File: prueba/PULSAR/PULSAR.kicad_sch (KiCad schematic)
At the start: 9 parts, among them J1 Conn_01x20, J2 Conn_01x04, J3 USB_C_Receptacle, U1 AP2112K-3.3, U2 SS49E, U3 CD74HC4067M, U4 ADS8688

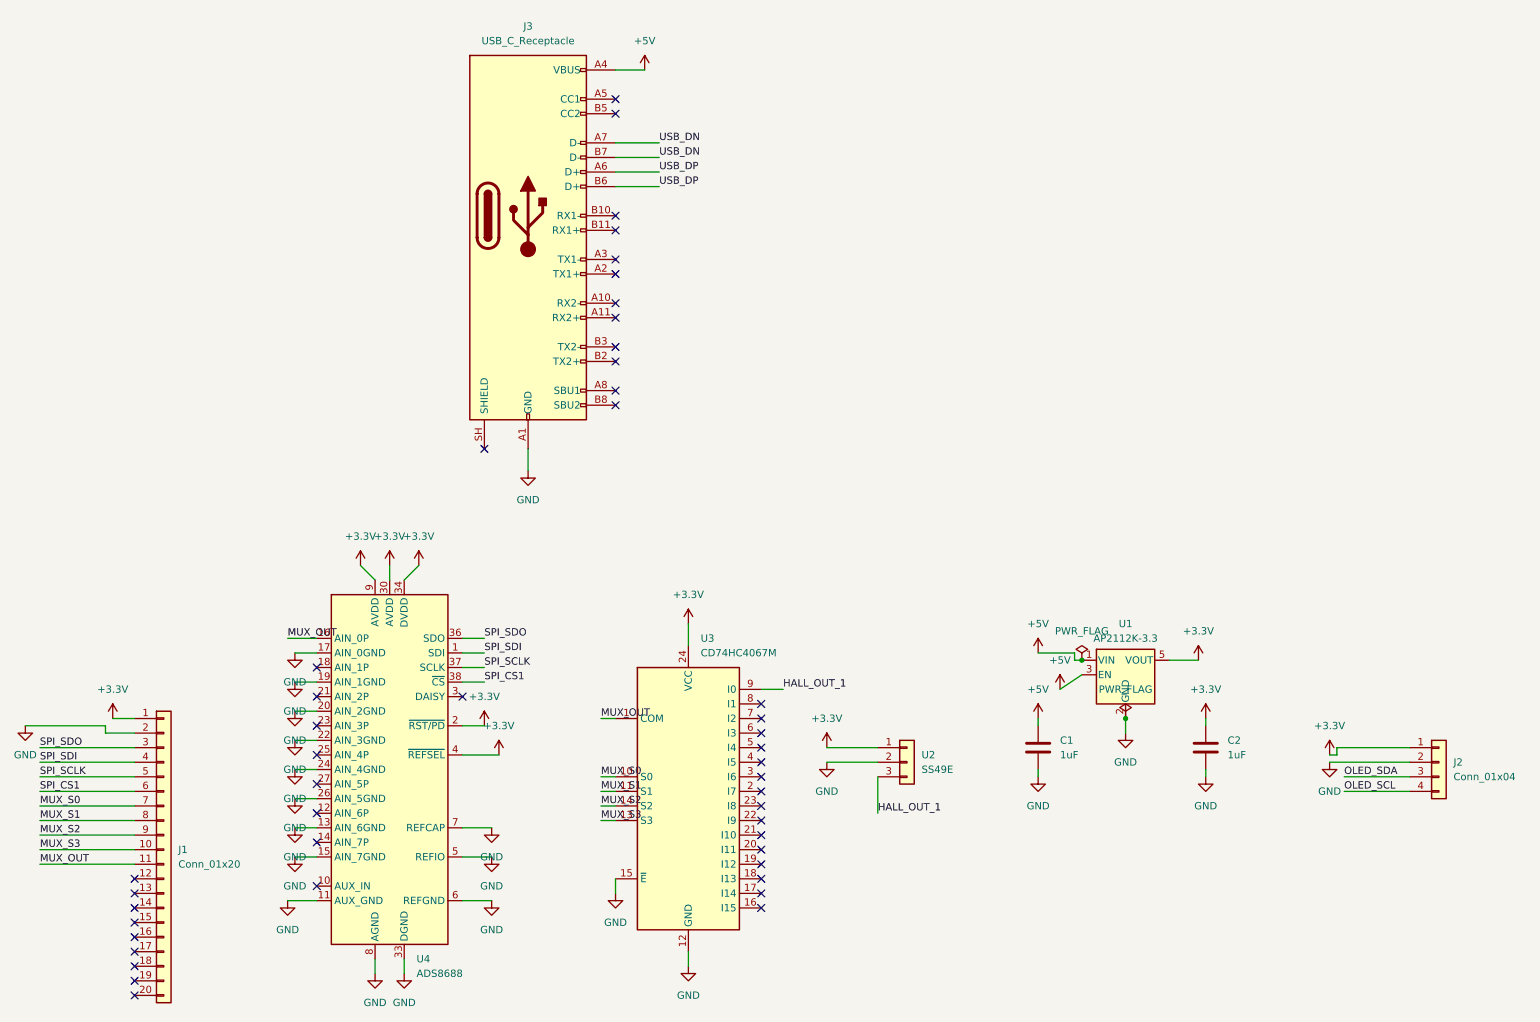
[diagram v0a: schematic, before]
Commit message: Kicad (#11)
* feat: esquemático base completo - USB-C, OLED SPI, OrangeCrab, ADS8688

* feat: complete BOM with verified LCSC part numbers

* feat: PCB routing in progress - power and SPI connections

---------

Co-authored-by: Axel Ibarrondo <135344010+Axel84727@users.noreply.github.com>
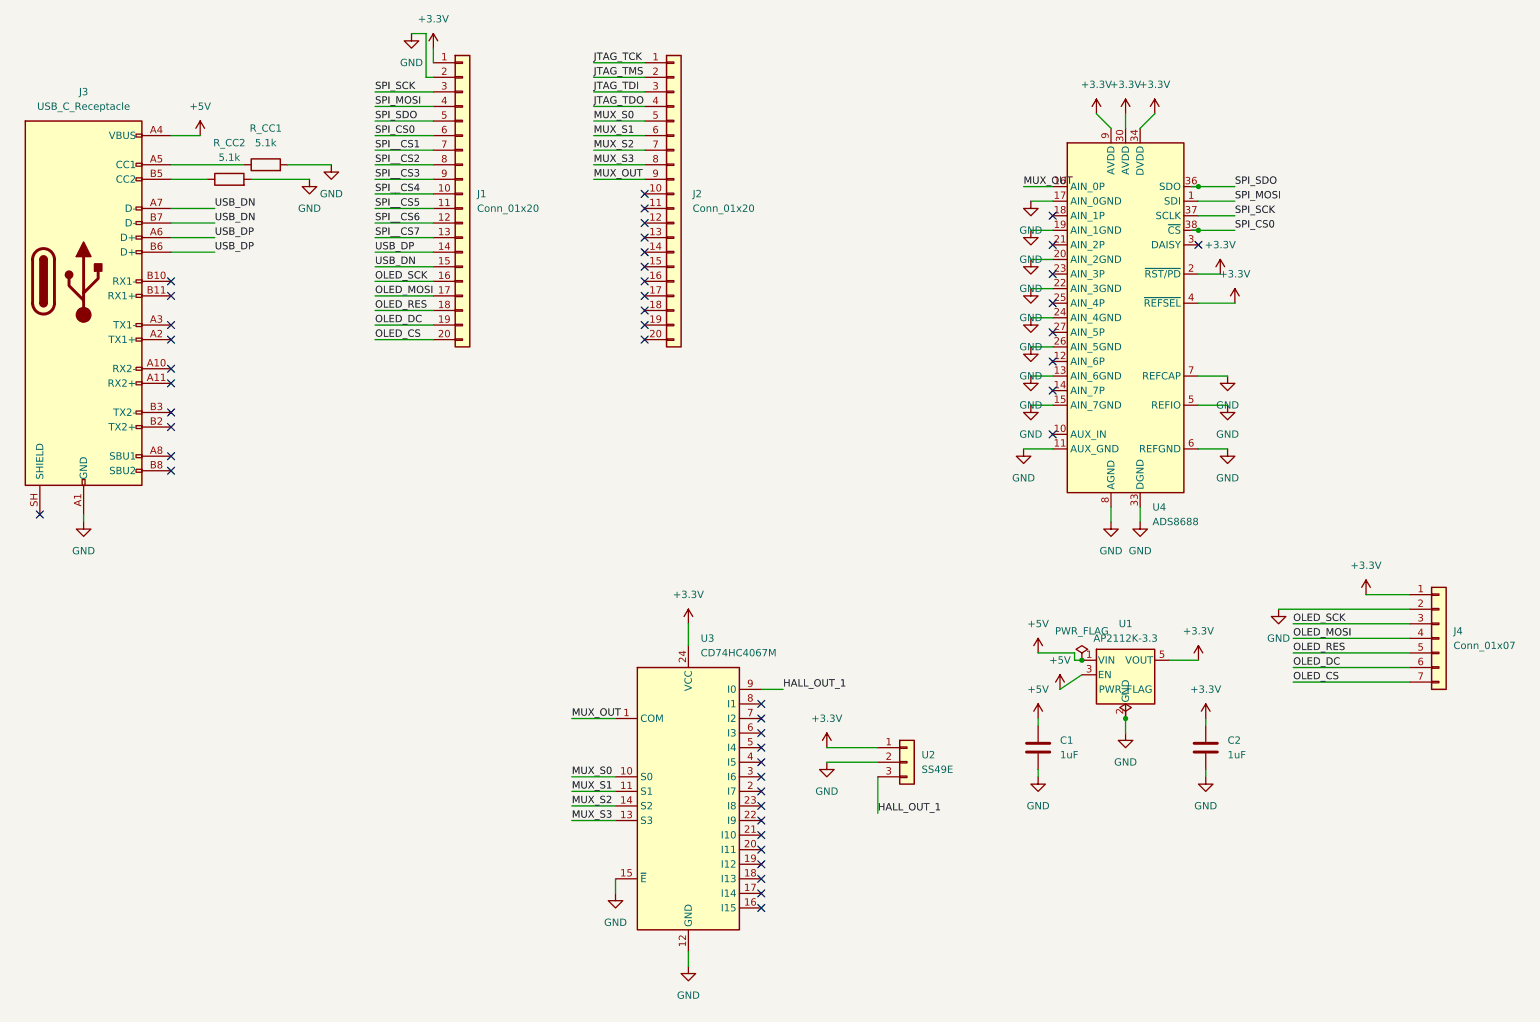
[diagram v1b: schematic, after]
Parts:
- removed J2: Conn_01x04, Connector_PinHeader_2.54mm:PinHeader_1x04_P2.54mm_Vertical, symbol Connector_Generic:Conn_01x04
- added J2: Conn_01x20, Connector_PinHeader_2.54mm:PinHeader_1x20_P2.54mm_Vertical, symbol Connector_Generic:Conn_01x20
- added J4: Conn_01x07, Connector_PinHeader_2.54mm:PinHeader_1x07_P2.54mm_Vertical, symbol Connector_Generic:Conn_01x07
- added R_CC1, R_CC2: 5.1k, Resistor_SMD:R_0402_1005Metric, symbol Device:R
- C1, C2: LCSC (none) -> C52923
- J1: now left out of the parts list
- J3: LCSC (none) -> C168688
- U1: LCSC (none) -> C51118
- U2: LCSC (none) -> C85697
- U3: footprint Package_SO:SOIC-24W_7.5x15.4mm_P1.27mm -> Package_SO:SSOP-24_5.3x8.2mm_P0.65mm; LCSC (none) -> C98457
- U4: LCSC (none) -> C1542682
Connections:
- net +3.3V: now also J4.1 (Pin_1)
- net GND: now also J4.2 (Pin_2), R_CC1.2, R_CC2.2
- net MUX_OUT: now also J2.9 (Pin_9); no longer J1.11 (Pin_11)
- net MUX_S0: now also J2.5 (Pin_5); no longer J1.7 (Pin_7)
- net MUX_S1: now also J2.6 (Pin_6); no longer J1.8 (Pin_8)
- net MUX_S2: now also J2.7 (Pin_7); no longer J1.9 (Pin_9)
- net MUX_S3: now also J2.8 (Pin_8); no longer J1.10 (Pin_10)
- net SPI_SDO: now also J1.5 (Pin_5); no longer J1.3 (Pin_3)
- net USB_DN: now also J1.15 (Pin_15)
- net USB_DP: now also J1.14 (Pin_14)
- net SPI__CS6: now reaches J1.12 (Pin_12)
- net SPI__CS7: now reaches J1.13 (Pin_13)
- net OLED_SCK: now reaches J1.16 (Pin_16)
- net OLED_SCK: now also J4.3 (Pin_3)
- net OLED_MOSI: now reaches J1.17 (Pin_17)
- net OLED_MOSI: now also J4.4 (Pin_4)
- net OLED_RES: now reaches J1.18 (Pin_18)
- net OLED_RES: now also J4.5 (Pin_5)
- net OLED_DC: now reaches J1.19 (Pin_19)
- net OLED_DC: now also J4.6 (Pin_6)
- net OLED_CS: now reaches J1.20 (Pin_20)
- net OLED_CS: now also J4.7 (Pin_7)
- net at J3.A5 (CC1): now also R_CC1.1
- net at J3.B5 (CC2): now also R_CC2.1
- net SPI_CS1 renamed SPI_CS0
- net SPI_SCLK renamed SPI_SCK
- net SPI_SCK: now also J1.3 (Pin_3); no longer J1.5 (Pin_5)
- net SPI_SDI renamed SPI_MOSI
- new net JTAG_TCK: J2.1 (Pin_1)
- new net JTAG_TDI: J2.3 (Pin_3)
- new net JTAG_TDO: J2.4 (Pin_4)
- new net JTAG_TMS: J2.2 (Pin_2)
- new net SPI__CS1: J1.7 (Pin_7)
- new net SPI__CS2: J1.8 (Pin_8)
- new net SPI__CS3: J1.9 (Pin_9)
- new net SPI__CS4: J1.10 (Pin_10)
- new net SPI__CS5: J1.11 (Pin_11)
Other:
- moved on the sheet: J3, U4
